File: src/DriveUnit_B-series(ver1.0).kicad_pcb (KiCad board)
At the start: 2 copper layers, 65.7 x 51 mm, 57 parts, among them IC1 A3921, SW1 TVAF06-A020B-R, SW2 TVAF06-A020B-R, SW3 THAF01-NC-R, SW4 SS-12D00G3

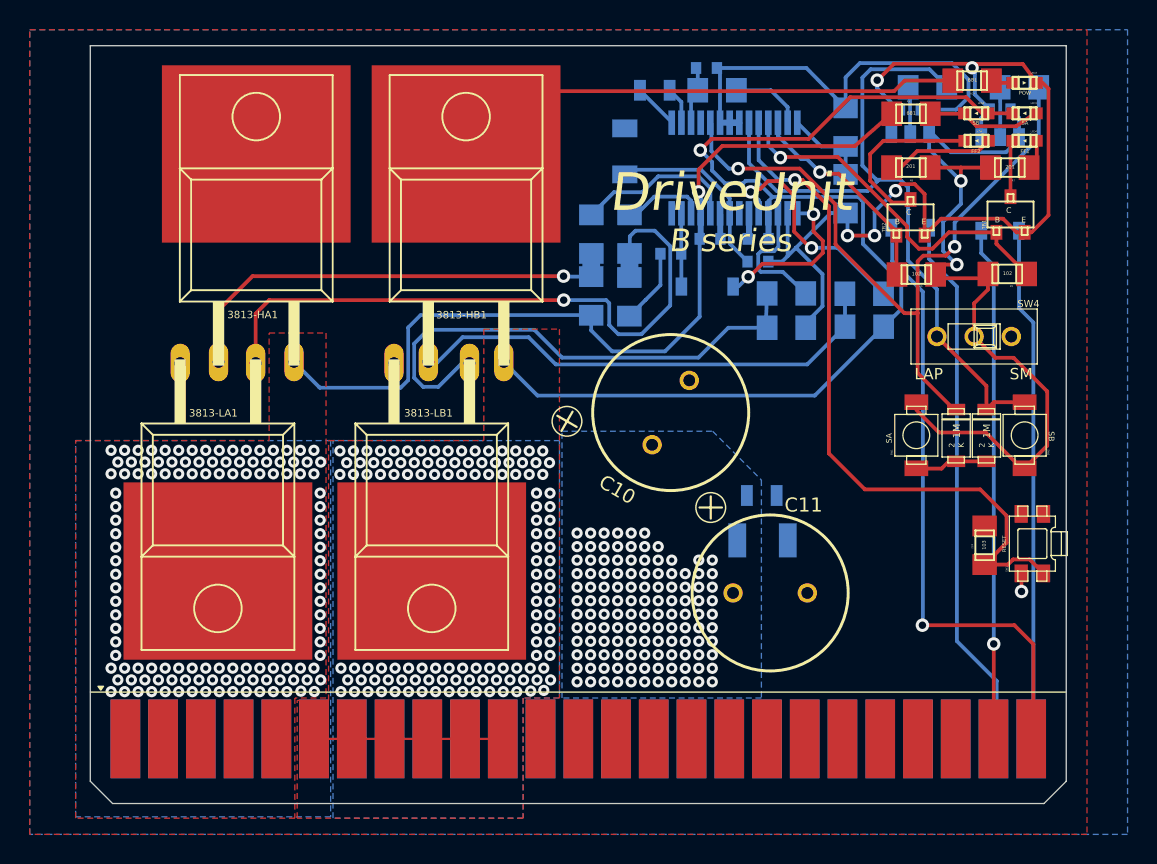
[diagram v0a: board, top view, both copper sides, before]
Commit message: 背面パッドの考慮
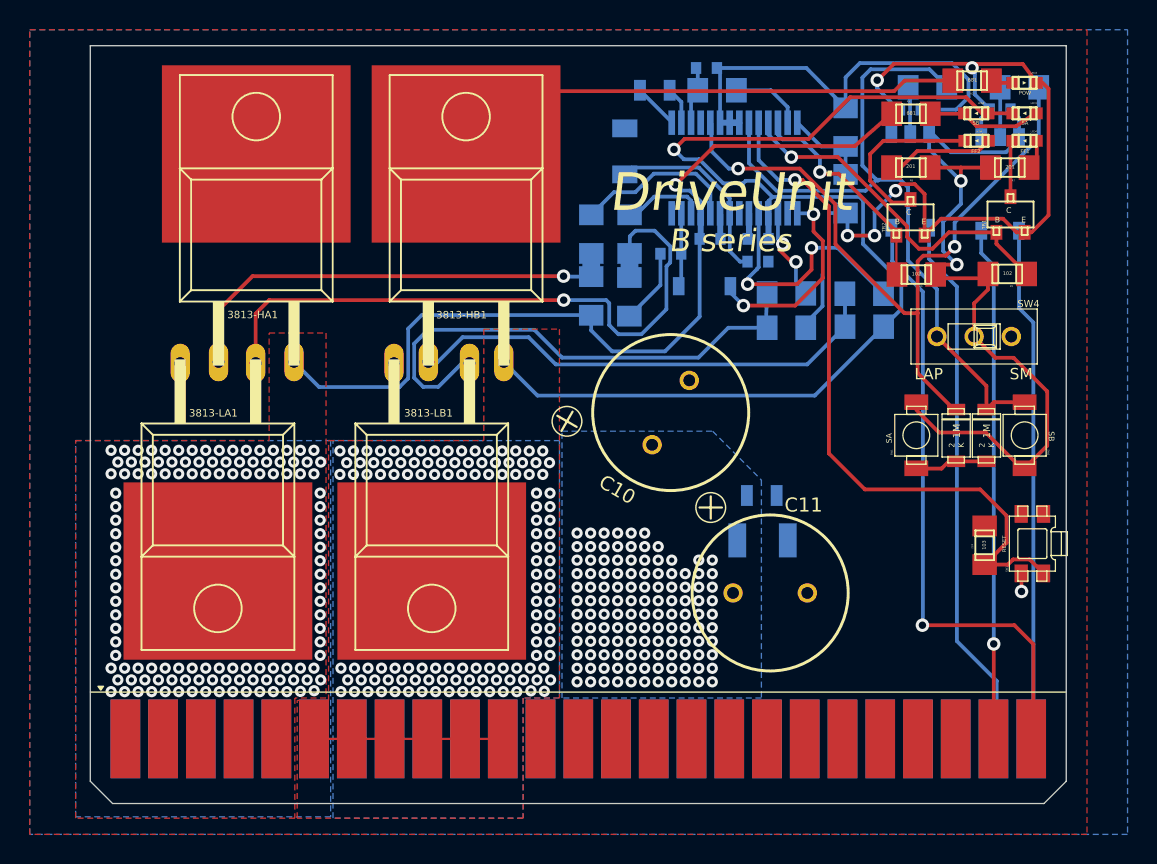
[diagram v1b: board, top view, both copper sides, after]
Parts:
- moved D1 0.18 mm to (155.3, 95.7)
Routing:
- net GND: track 82.4 -> 68.5 mm
- net VCC: track 53.9 -> 50.2 mm
- net /GLB: track 8.97 -> 6.55 mm, vias 0 -> 2
- net /SB: track 99.2 -> 97.0 mm
- net /GHB: track 15.5 -> 17.4 mm
- net /SA: track 59.3 -> 60.9 mm
- net /FF2: track 14.4 -> 15.0 mm

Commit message: ガバ設計による炎上回避(GNDベタを大きくした)
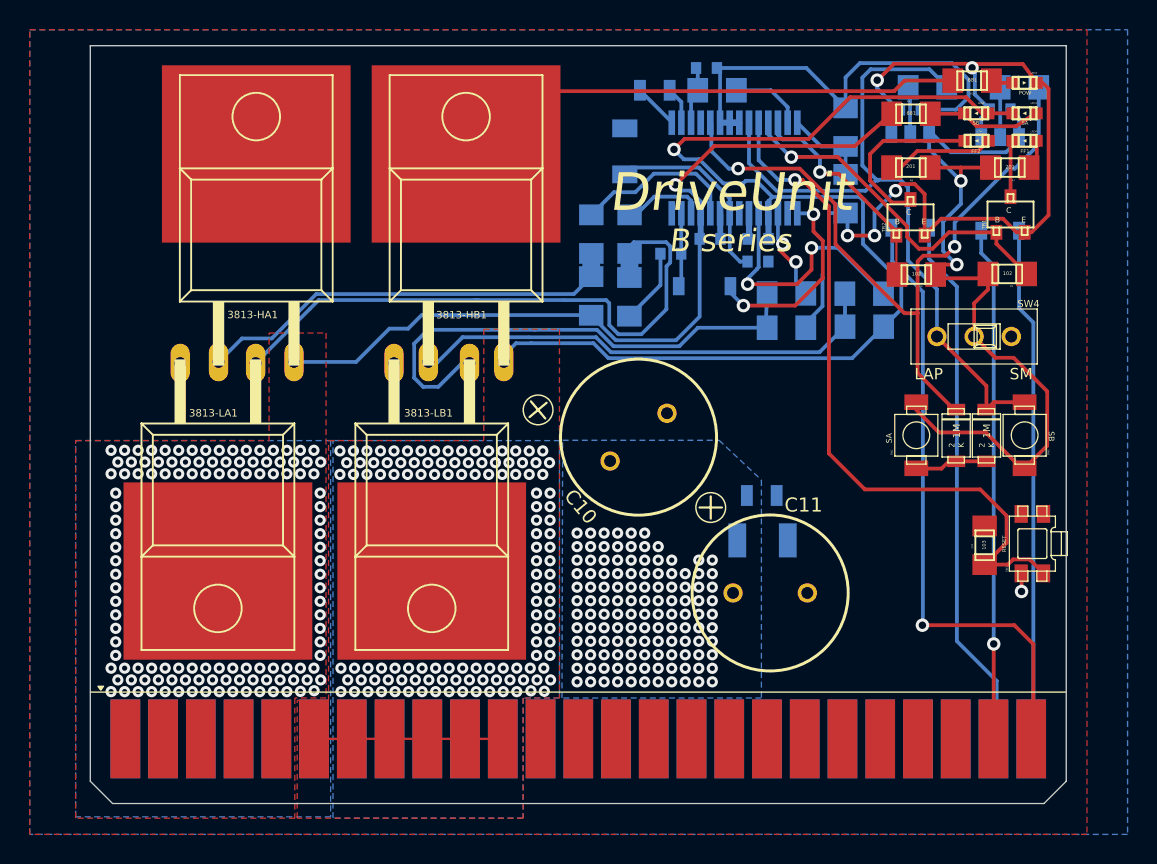
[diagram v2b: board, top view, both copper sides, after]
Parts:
- moved C10 2.72 mm to (152.6, 105.8), turned to 130 degrees
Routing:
- net /SA: track 60.9 -> 56.4 mm
- net Net-(3813-LA1-PadGATE): track 44.3 -> 41.6 mm, vias 1 -> 0
- net Net-(3813-HA1-PadGATE): track 31.1 -> 29.0 mm, vias 1 -> 0
- net /SB: track 97.0 -> 96.3 mm
- net Net-(3813-HB1-PadGATE): track 32.8 -> 32.1 mm
- net Net-(3813-LB1-PadGATE): track 35.1 -> 34.4 mm

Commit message: シルクの修正
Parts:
- moved C10 2.39 mm to (152.3, 108.2), turned to 140 degrees
- moved C13 1.88 mm to (159.0, 110.2), turned to 52 degrees
- moved C12 1.28 mm to (161.3, 114.0)
- moved C11 1.00 mm to (162.1, 117.1)
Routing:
- net /SB: vias 123 -> 75
- net /SA: vias 123 -> 75
